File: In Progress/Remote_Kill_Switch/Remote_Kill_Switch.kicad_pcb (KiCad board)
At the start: 2 copper layers, 3 parts, among them U2 LTC4054ES5-4.2, U4 CP2104, U5 UMH3N

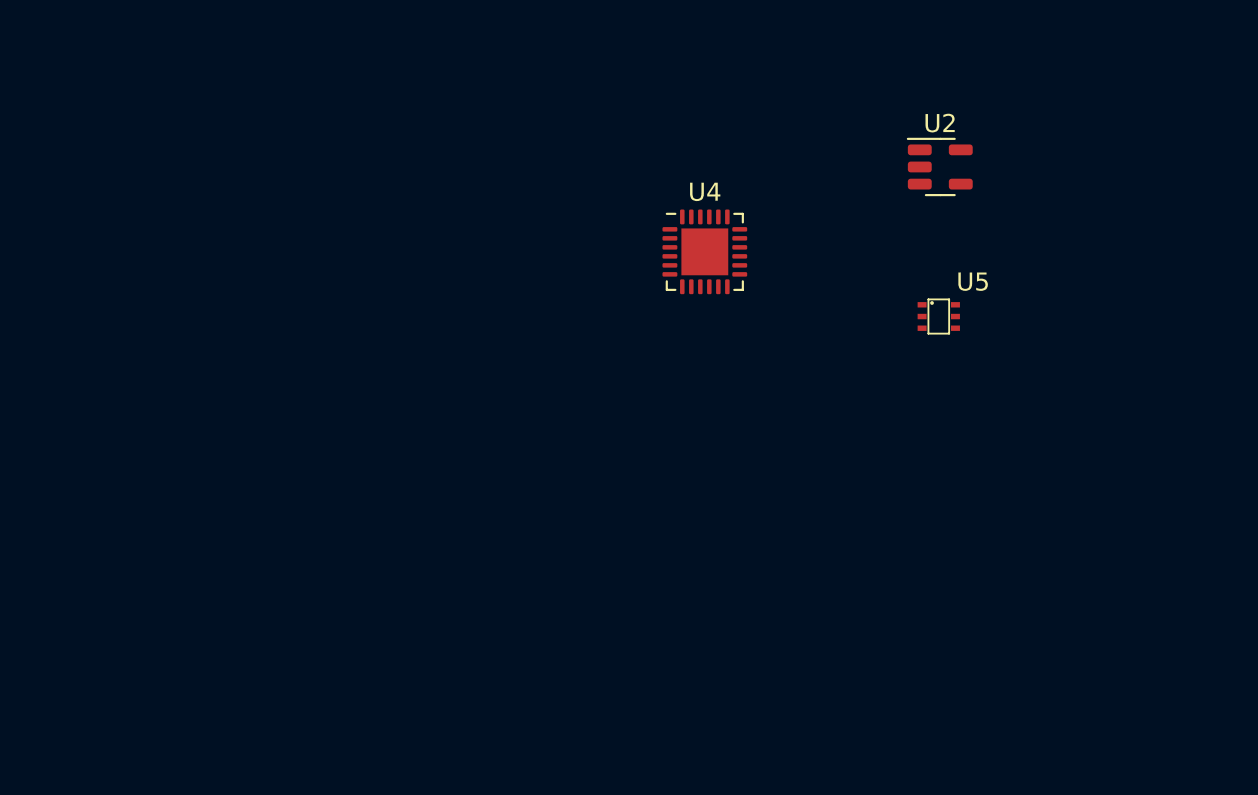
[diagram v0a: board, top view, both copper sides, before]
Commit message: Added custom libraries and updated the Kill Switch (Remote)
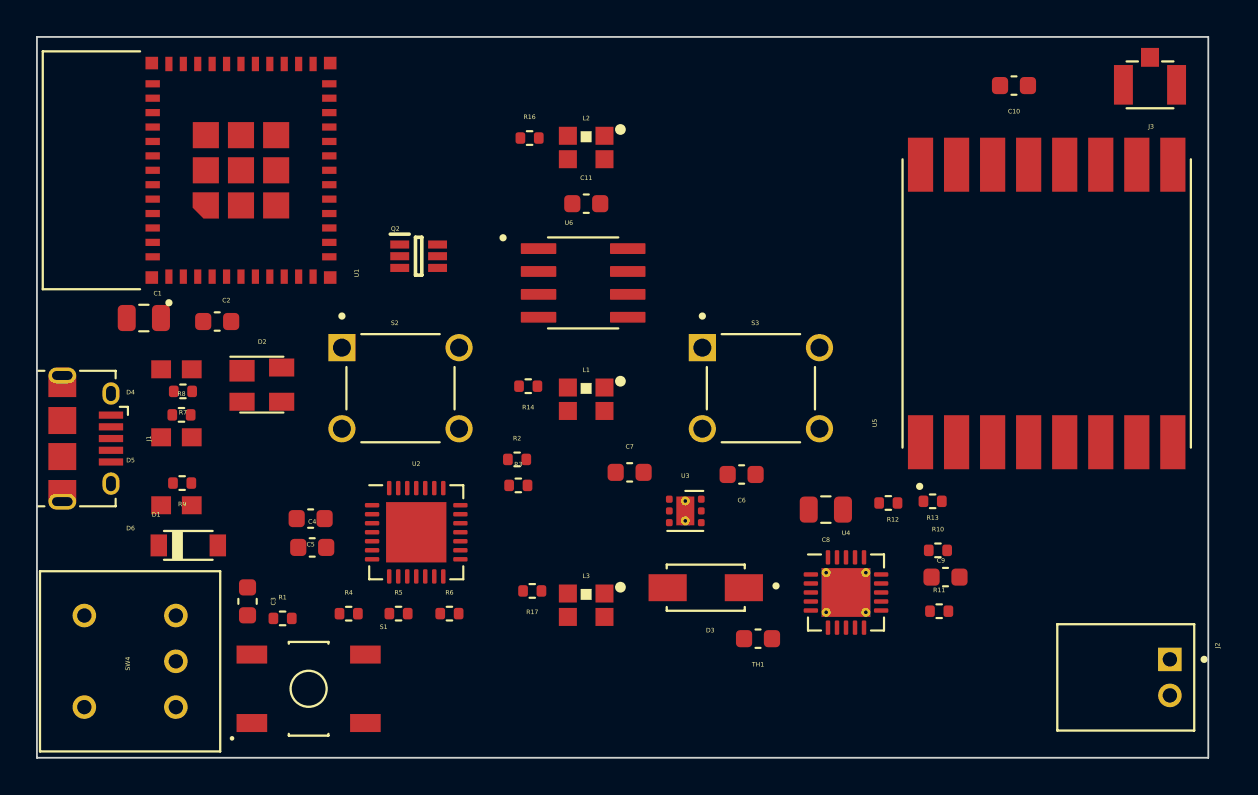
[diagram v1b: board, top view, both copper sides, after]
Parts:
- added C1: 10uF, Capacitor_SMD:C_0805_2012Metric, F.Cu at (90.9, 85.6)
- added C10: .1uF, Capacitor_SMD:C_0603_1608Metric, F.Cu at (139.2, 72.7)
- added C11: .1uF, Capacitor_SMD:C_0603_1608Metric, F.Cu at (115.5, 79.3)
- added C2: .1uF, Capacitor_SMD:C_0603_1608Metric, F.Cu at (95.0, 85.8)
- added C3: .1uF, Capacitor_SMD:C_0603_1608Metric, F.Cu at (96.7, 101.3)
- added C4: 4.7uF, Capacitor_SMD:C_0603_1608Metric, F.Cu at (100.3, 98.3)
- added C5: .1uF, Capacitor_SMD:C_0603_1608Metric, F.Cu at (100.2, 96.7)
- added C6: 1uF, Capacitor_SMD:C_0603_1608Metric, F.Cu at (124.1, 94.3)
- added C7: 1uF, Capacitor_SMD:C_0603_1608Metric, F.Cu at (117.9, 94.2)
- added C8: 10uF, Capacitor_SMD:C_0805_2012Metric, F.Cu at (128.8, 96.2)
- added C9: 4.7uF, Capacitor_SMD:C_0603_1608Metric, F.Cu at (135.4, 100.0)
- added D1: B5819W-TP, Custom:SOD3716X135N, F.Cu at (93.4, 98.2)
- added D2: SP0503BAHTG, Package_TO_SOT_SMD:SOT-143, F.Cu at (97.5, 89.3)
- added D3: SMAJ5.0, Custom:SMAJ5.0_DIOM4325X250N, F.Cu at (122.1, 100.6)
- added D4: Green, Custom:LED_0603, F.Cu at (92.7, 88.4)
- added D5: BLUE, Custom:LED_0603, F.Cu at (92.7, 92.2)
- added D6: Red, Custom:LED_0603, F.Cu at (92.7, 96.0)
- added J1: USB_B_Micro, Connector_USB:USB_Micro-B_Amphenol_10118194_Horizontal, F.Cu at (87.7, 92.3)
- added J2: S2B-PH-K-S(LF)(SN), Custom:JST_S2B-PH-K-S(LF)(SN), F.Cu at (147.9, 105.5)
- added J3: U.FL-R-SMT-1(10), Custom:HRS_U.FL-R-SMT-1(10), F.Cu at (146.8, 72.7)
- added L1: WS2812B-2020, Custom:WS2812B-2020, F.Cu at (115.5, 90.1)
- added L2: WS2812B-2020, Custom:WS2812B-2020, F.Cu at (115.5, 76.1)
- added L3: WS2812B-2020, Custom:WS2812B-2020, F.Cu at (115.5, 101.5)
- added Q2: UMH3N, Custom:SOT65P230X110-6N, F.Cu at (106.2, 82.2)
- added R1: 10K, Resistor_SMD:R_0402_1005Metric, F.Cu at (98.6, 102.3)
- added R10: 10K, Resistor_SMD:R_0402_1005Metric, F.Cu at (135.0, 98.5)
- added R11: 100K, Resistor_SMD:R_0402_1005Metric, F.Cu at (135.1, 101.9)
- added R12: 100K, Resistor_SMD:R_0402_1005Metric, F.Cu at (132.2, 95.9)
- added R13: 100K, Resistor_SMD:R_0402_1005Metric, F.Cu at (134.7, 95.8)
- added R14: 470, Resistor_SMD:R_0402_1005Metric, F.Cu at (112.3, 89.4)
- added R16: 470, Resistor_SMD:R_0402_1005Metric, F.Cu at (112.3, 75.6)
- added R17: 470, Resistor_SMD:R_0402_1005Metric, F.Cu at (112.5, 100.7)
- added R2: 1K, Resistor_SMD:R_0402_1005Metric, F.Cu at (111.6, 93.4)
- added R3: 1K, Resistor_SMD:R_0402_1005Metric, F.Cu at (111.7, 94.9)
- added R4: 22.1K, Resistor_SMD:R_0402_1005Metric, F.Cu at (102.3, 102.0)
- added R5: 47.5K, Resistor_SMD:R_0402_1005Metric, F.Cu at (105.1, 102.0)
- added R6: 1K, Resistor_SMD:R_0402_1005Metric, F.Cu at (107.9, 102.0)
- added R7: 82, Resistor_SMD:R_0402_1005Metric, F.Cu at (93.1, 89.7)
- added R8: 82, Resistor_SMD:R_0402_1005Metric, F.Cu at (93.0, 91.0)
- added R9: 150, Resistor_SMD:R_0402_1005Metric, F.Cu at (93.1, 94.8)
- added S1: TL3342F160QG, Custom:SW_TL3342F160QG, F.Cu at (100.1, 106.2)
- added S2: TS02-66-100-BK-100-LCR-D, Custom:SW_TS02-66-100-BK-100-LCR-D, F.Cu at (105.2, 89.5)
- added S3: TS02-66-100-BK-100-LCR-D, Custom:SW_TS02-66-100-BK-100-LCR-D, F.Cu at (125.2, 89.5)
- added SW4: AS11CH, Custom:AS11CH, F.Cu at (90.2, 104.6)
- added TH1: 10K, Capacitor_SMD:C_0603_1608Metric, F.Cu at (125.0, 103.4)
- added U1: ESP32-PICO-MINI-02, Custom:MODULE_ESP32-PICO-MINI-02, F.Cu at (96.3, 77.4)
- added U3: LP5912-3.3DRV, Package_SON:WSON-6-1EP_2x2mm_P0.65mm_EP1x1.6mm_ThermalVias, F.Cu at (121.0, 96.3)
- added U6: LS18-S(Debouce), Custom:SOIC127P600X175-8N, F.Cu at (115.3, 83.7)
- U2: value LTC4054ES5-4.2 -> CP2102N-A02-GQFN28; footprint Package_TO_SOT_SMD:TSOT-23-5 -> Package_DFN_QFN:QFN-28-1EP_5x5mm_P0.5mm_EP3.35x3.35mm
- U4: value CP2104 -> MCP73871-2CC-Custom; footprint Package_DFN_QFN:QFN-24-1EP_4x4mm_P0.5mm_EP2.6x2.6mm -> Package_DFN_QFN:QFN-20-1EP_4x4mm_P0.5mm_EP2.7x2.7mm_ThermalVias
- U5: value UMH3N -> RFM95W-915S2; footprint Custom:UMT6 -> Custom:RFM95W-915S2
- moved U2 35.4 mm to (106.0, 97.5)
- moved U4 20.5 mm to (129.9, 100.8)
- moved U5 6.03 mm to (141.0, 84.8), turned to 90 degrees
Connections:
- U2 pad 3: unconnected-(U2-Pad3) -> GND
- U2 pad 4: unconnected-(U2-Pad4) -> USB_DP
- U2 pad 5: unconnected-(U2-Pad5) -> USB_DN
- U4 pad 1: unconnected-(U4-Pad1) -> Net-(C6-Pad2)
- U4 pad 10: unconnected-(U4-Pad10) -> GND
- U4 pad 11: unconnected-(U4-Pad11) -> GND
- U4 pad 12: unconnected-(U4-Pad12) -> Net-(R11-Pad1)
- U4 pad 13: unconnected-(U4-Pad13) -> Net-(R10-Pad1)
- U4 pad 14: unconnected-(U4-Pad14) -> Net-(C9-Pad1)
- U4 pad 15: unconnected-(U4-Pad15) -> Net-(C9-Pad1)
- U4 pad 16: unconnected-(U4-Pad16) -> Net-(C9-Pad1)
- U4 pad 17: unconnected-(U4-Pad17) -> VBUS
- U4 pad 18: unconnected-(U4-Pad18) -> VBUS
- U4 pad 19: unconnected-(U4-Pad19) -> VBUS
- U4 pad 2: Net-(U4-Pad2) -> VBUS
- U4 pad 20: unconnected-(U4-Pad20) -> Net-(C6-Pad2)
- U4 pad 21: unconnected-(U4-Pad21) -> (no net)
- U4 pad 3: unconnected-(U4-Pad3) -> GND
- U4 pad 4: unconnected-(U4-Pad4) -> GND
- U4 pad 5: unconnected-(U4-Pad5) -> Net-(TH1-Pad1)
- U4 pad 6: unconnected-(U4-Pad6) -> Net-(R7-Pad1)
- U4 pad 7: unconnected-(U4-Pad7) -> Net-(U4-Pad7)
- U4 pad 8: unconnected-(U4-Pad8) -> Net-(R9-Pad1)
- U4 pad 9: unconnected-(U4-Pad9) -> GND
- U5 pad 1: unconnected-(U5-Pad1) -> GND
- U5 pad 2: unconnected-(U5-Pad2) -> MISO_LORA
- U5 pad 3: unconnected-(U5-Pad3) -> MOSI_LORA
- U5 pad 4: unconnected-(U5-Pad4) -> SCK_LORA
- U5 pad 5: unconnected-(U5-Pad5) -> NSS_LORA
- U5 pad 6: unconnected-(U5-Pad6) -> RESET_LORA
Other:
- board outline added: 65 x 40 mm
